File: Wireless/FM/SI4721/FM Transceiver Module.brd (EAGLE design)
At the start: 34.3 x 25.4 mm, 29 parts, among them CN1 35RASMT4BHNTRX, U1 SI4721, Y1 CRYSTAL.ABS07

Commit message: Completed schematic for FM Transceiver (SI4721) Layout completed. Routing needed...
Signed-off-by: Cruz Monrreal II <Cruz.Monrreal@gmail.com>
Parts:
- added C13: 1uF, .standardparts:0603
- added C14: .1uF, .standardparts:0603
- added C4: 22uF, .standardparts:0805
- added J1, J2: (no value), .solderjumper:3.LRG.12
- added J10, J11, J12, J13, J14, J15, J16, J17, J18, J3, J4, J5, J6, J7, J8, J9: (no value), .solderjumper:2.SML
- added R1, R8: 20k, .standardparts:0603
- added U$7: TPA6111.DGN, .packages(ti):DGN
- moved FB2 95.4 mm to (22.9, 9.53), turned to 270 degrees
- moved FB1 91.7 mm to (22.9, 6.35), turned to 270 degrees
- moved R7 82.0 mm to (12.7, 18.4), turned to 270 degrees
- moved R6 77.8 mm to (11.4, 18.4), turned to 270 degrees
- moved C12 73.2 mm to (19.1, 9.53), turned to 270 degrees
- moved R5 72.5 mm to (8.89, 18.4), turned to 270 degrees
- moved R4 70.8 mm to (10.2, 18.4), turned to 270 degrees
- moved C11 69.3 mm to (19.1, 6.35), turned to 270 degrees
- moved C10 68.3 mm to (20.3, 9.53), turned to 90 degrees
- moved C9 64.4 mm to (20.3, 6.35), turned to 90 degrees
- moved R3 63.5 mm to (21.6, 9.53), turned to 90 degrees
- moved R2 59.5 mm to (21.6, 6.35), turned to 90 degrees
- moved C8 52.1 mm to (12.7, 15.9), turned to 270 degrees
- moved C7 48.3 mm to (11.4, 15.9), turned to 270 degrees
- moved C6 43.6 mm to (8.89, 15.9), turned to 270 degrees
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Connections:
- removed net !SEN!: U1.6
- removed net N$1: U$2.04, U$2.04@1, U$2.04@VIA
- removed net N$10: U$2.01, U$2.01@1, U$2.01@VIA
- removed net N$11: U$2.02, U$2.02@1, U$2.02@VIA
- removed net N$14: U$2.05, U$2.05@1, U$2.05@VIA
- removed net N$15: U$2.06, U$2.06@1, U$2.06@VIA
- removed net N$16: U$2.07, U$2.07@1, U$2.07@VIA
- removed net N$17: U$2.WAKE, U$2.WAKE@1, U$2.WAKE@VIA
- removed net N$4: U$2.SCL, U$2.SCL@1, U$2.SCL@VIA
- removed net N$5: U$2.03, U$2.03@1, U$2.03@VIA
- removed net SCLK: U1.7
- removed net SDIO: U1.8
- new net 01: J11.1, J3.1, U$2.01, U$2.01@1, U$2.01@VIA
- new net 02: J12.1, J4.1, U$2.02, U$2.02@1, U$2.02@VIA
- new net 03: J13.1, J5.1, U$2.03, U$2.03@1, U$2.03@VIA
- new net 04: J14.1, J6.1, U$2.04, U$2.04@1, U$2.04@VIA
- new net 05: J15.1, J7.1, U$2.05, U$2.05@1, U$2.05@VIA
- new net 06: J16.1, J8.1, U$2.06, U$2.06@1, U$2.06@VIA
- new net 07: J17.1, J9.1, U$2.07, U$2.07@1, U$2.07@VIA
- new net 08: J10.1, J18.1, U$2.WAKE, U$2.WAKE@1, U$2.WAKE@VIA
- new net LOUT.AMP: C7.2, U1.14
- new net N$26: R7.1, R8.2, U$7.2
- new net N$39: R1.2, R6.1, U$7.6
- new net N$42: J2.1, R5.1
- new net N$43: J1.1, R4.1
- new net ROUT.AMP: C8.2, U1.13
- new net SCL: U$2.SCL, U$2.SCL@1, U$2.SCL@VIA, U1.7
- new net SDA: U$2.SDA, U$2.SDA@1, U$2.SDA@VIA, U1.8
- new net SHDN: J11.2, J12.2, J13.2, J14.2, J15.2, J16.2, J17.2, J18.2, U$7.5
- net 3.3V: now also C14.1, C4.2, U$7.8
- net GND: now also C13.2, C14.2, C4.1, U$7.4, U$7.PAD, U1.6
- net LOUT: now also J2.3, R1.1, U$7.7; no longer C8.2, U1.14
- net N$29: now also J1.2
- net N$3: now also C13.1, U$7.3; no longer U$2.SDA, U$2.SDA@1, U$2.SDA@VIA
- net N$32: now also J2.2
- net ROUT: now also J1.3, R8.1, U$7.1; no longer C7.2, U1.13
- net RST: now also J10.2, J3.2, J4.2, J5.2, J6.2, J7.2, J8.2, J9.2
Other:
- board text added: "ANT"
- board text added: "AnomalousMaker.com"
- board text added: "Transmitter Receiver"
- board text removed: "InnovativeMaker.com"

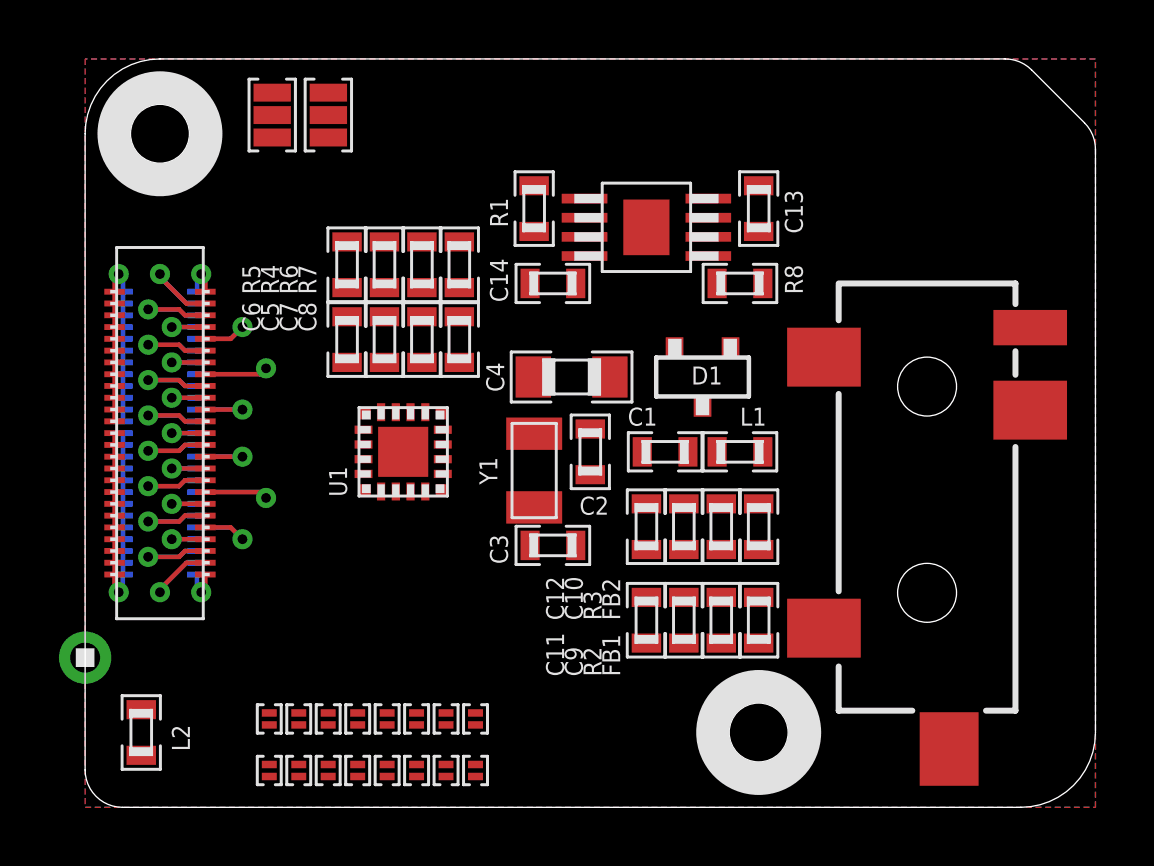
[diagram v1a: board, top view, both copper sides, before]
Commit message: Completed FM Transceiver Module
Signed-off-by: Cruz Monrreal II <Cruz.Monrreal@gmail.com>
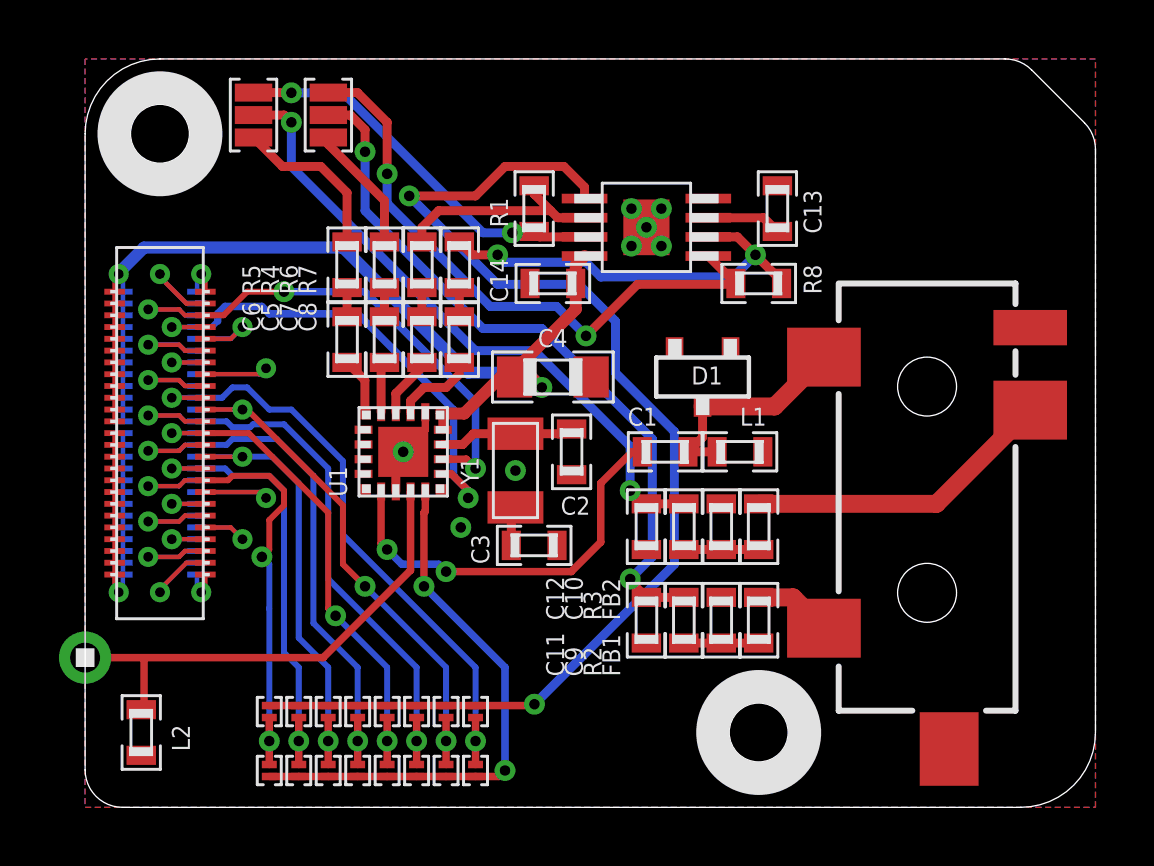
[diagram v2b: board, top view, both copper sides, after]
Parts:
- moved C13 0.64 mm to (23.5, 20.3)
- moved C4 0.64 mm to (15.9, 14.6)
- moved C3 0.63 mm to (15.2, 8.89)
- moved J2 0.63 mm to (5.71, 23.5)
- moved Y1 0.63 mm to (14.6, 11.4)
- moved C2 0.63 mm to (16.5, 12.1)
- moved R8 0.63 mm to (22.9, 17.8)
- moved J11 0.25 mm to (13.2, 3.25)
- moved J12 0.25 mm to (12.2, 3.25)
- moved J13 0.25 mm to (11.2, 3.25)
- moved J14 0.25 mm to (10.2, 3.25)
- moved J15 0.25 mm to (9.25, 3.25)
- moved J16 0.25 mm to (8.25, 3.25)
- moved J17 0.25 mm to (7.25, 3.25)
- moved J18 0.25 mm to (6.25, 3.25)
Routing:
- net SHDN: track 0.00 -> 40.6 mm, vias 0 -> 2
- net 3.3V: track 0.00 -> 26.4 mm, vias 0 -> 1
- net N$29: track 0.00 -> 24.3 mm, vias 0 -> 2
- net N$32: track 0.00 -> 21.8 mm, vias 0 -> 2
- net ROUT: track 0.00 -> 20.9 mm, vias 0 -> 2
- net 01: track 0.00 -> 19.1 mm, vias 0 -> 1
- net RST: track 0.00 -> 18.7 mm, vias 0 -> 2
- net 03: track 0.00 -> 17.3 mm, vias 0 -> 1
- net TXO: track 0.00 -> 16.8 mm
- net 02: track 0.00 -> 15.8 mm, vias 0 -> 2
- net 05: track 0.00 -> 15.8 mm, vias 0 -> 1
- net 04: track 0.00 -> 15.5 mm, vias 0 -> 2
- net SCL: track 0.00 -> 15.1 mm, vias 0 -> 1
- net SDA: track 0.00 -> 14.5 mm, vias 0 -> 2
- net N$26: track 0.00 -> 14.0 mm, vias 0 -> 2
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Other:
- board text added: "01"
- board text added: "02"
- board text added: "03"
- board text added: "04"
- board text added: "05"
- board text added: "06"
- board text added: "07"
- board text added: "08"
- board text added: "RST"
- board text added: "SHDN"

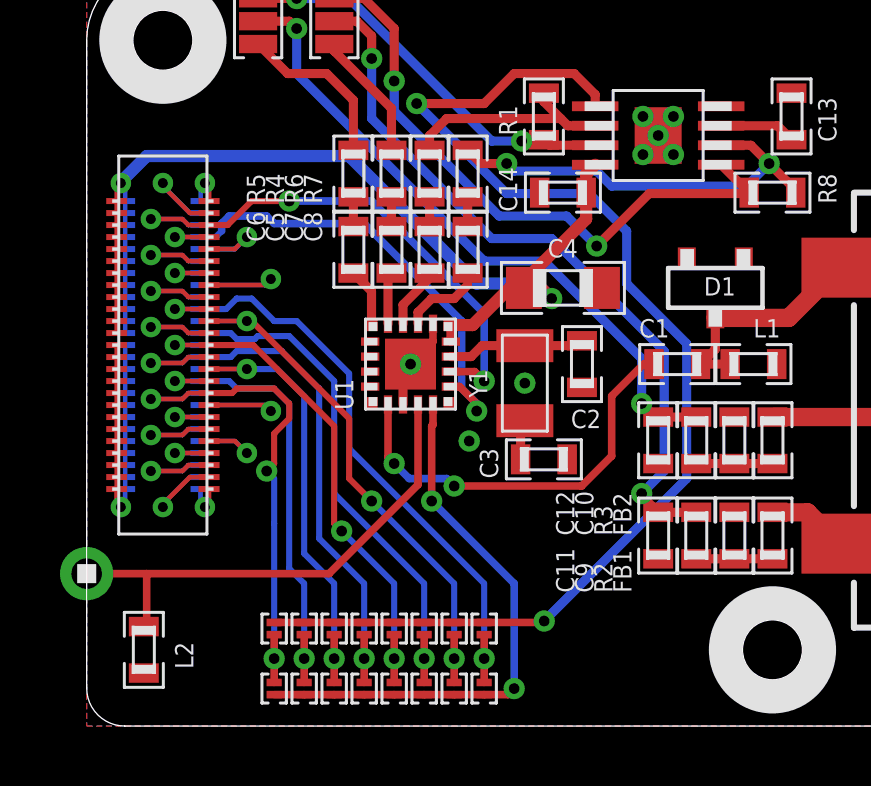
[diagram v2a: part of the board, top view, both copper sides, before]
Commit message: Tweaked bottom silkscreen and added more GND Plane space
Signed-off-by: Cruz Monrreal II <Cruz.Monrreal@gmail.com>
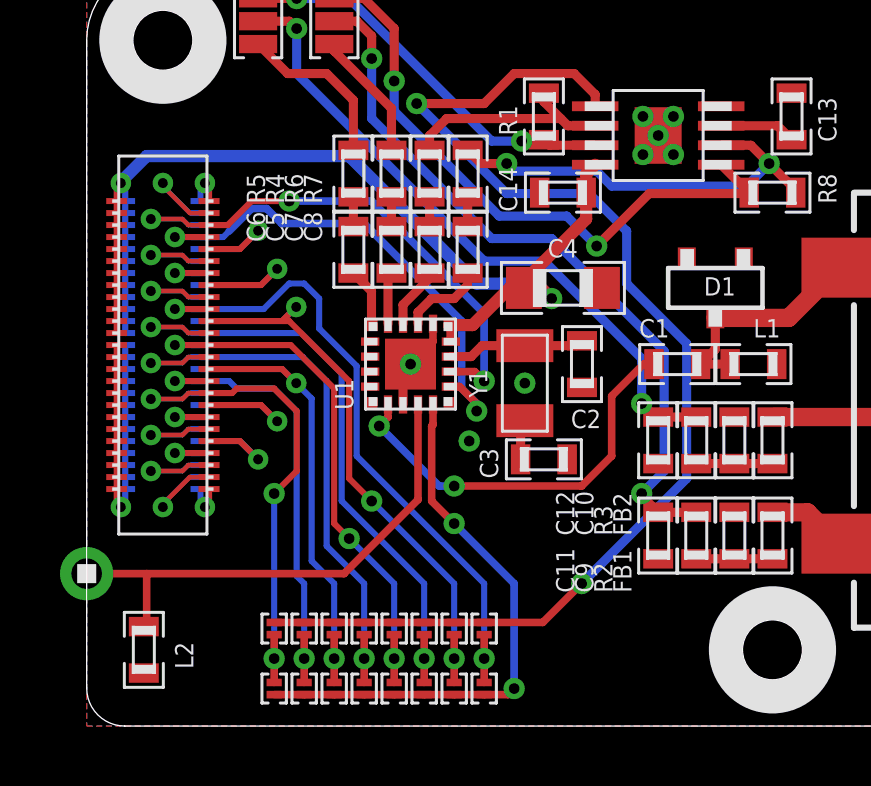
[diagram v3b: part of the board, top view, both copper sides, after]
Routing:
- net 06: track 13.0 -> 11.3 mm
- net 01: track 19.1 -> 20.4 mm
- net 04: track 15.5 -> 16.2 mm
- net N$12: track 1.71 -> 1.15 mm
- net SCL: track 15.1 -> 15.7 mm
